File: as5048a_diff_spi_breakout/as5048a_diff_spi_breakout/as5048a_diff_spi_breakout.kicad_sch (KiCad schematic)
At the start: 8 parts, among them J1 Conn_01x02, J2 8P8C, U1 SN65LVDT14, U2 AS5048A

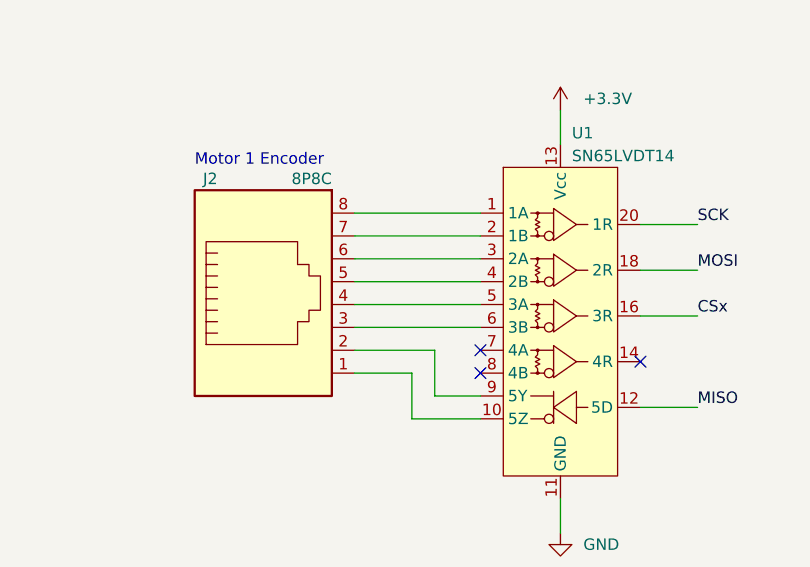
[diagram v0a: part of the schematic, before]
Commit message: adding pareto leg kins
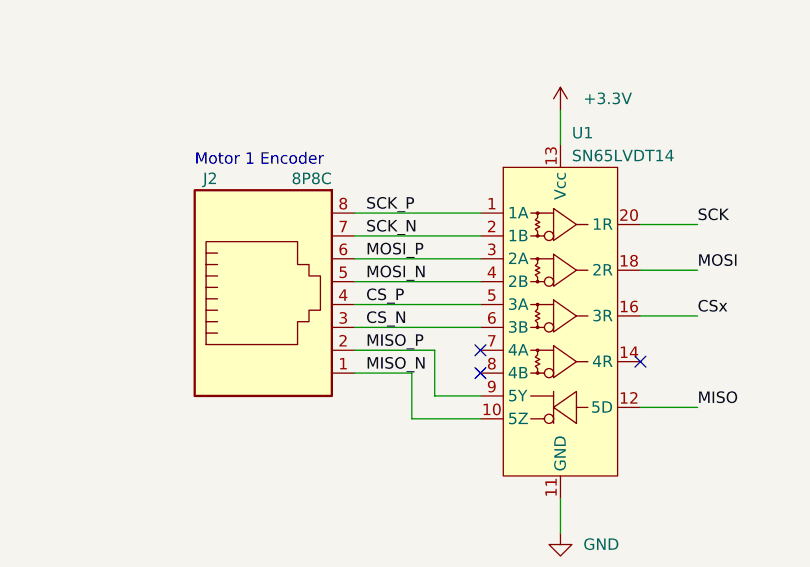
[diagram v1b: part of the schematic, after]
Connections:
- net SCK_P: now reaches J2.8, U1.1 (1A)
- net MISO_N: now reaches J2.1, U1.10 (5Z)
- net SCK_N: now reaches J2.7, U1.2 (1B)
- net MOSI_P: now reaches J2.6, U1.3 (2A)
- net MOSI_N: now reaches J2.5, U1.4 (2B)
- net CS_P: now reaches J2.4, U1.5 (3A)
- net CS_N: now reaches J2.3, U1.6 (3B)
- net MISO_P: now reaches J2.2, U1.9 (5Y)
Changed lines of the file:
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@@
+    (effects (font (size 1.27 1.27)) (justify left bottom))
+  )
+  (label "MISO_P" (at 105.41 97.79 0)
     (effects (font (size 1.27 1.27)) (justify left bottom))
   )
@@
   )
   (label "CSx" (at 142.24 93.98 0)
+    (effects (font (size 1.27 1.27)) (justify left bottom))
+  )
+  (label "MISO_N" (at 105.41 100.33 0)
     (effects (font (size 1.27 1.27)) (justify left bottom))
   )
@@
     (effects (font (size 1.27 1.27)) (justify left bottom))
   )
+  (label "SCK_N" (at 105.41 85.09 0)
+    (effects (font (size 1.27 1.27)) (justify left bottom))
+  )
   (label "MISO" (at 142.24 104.14 0)
+    (effects (font (size 1.27 1.27)) (justify left bottom))
+  )
+  (label "CS_P" (at 105.41 92.71 0)
+    (effects (font (size 1.27 1.27)) (justify left bottom))
+  )
+  (label "CS_N" (at 105.41 95.25 0)
+    (effects (font (size 1.27 1.27)) (justify left bottom))
+  )
+  (label "MOSI_N" (at 105.41 90.17 0)
     (effects (font (size 1.27 1.27)) (justify left bottom))
   )
@@
     (effects (font (size 1.27 1.27)) (justify left bottom))
   )
+  (label "SCK_P" (at 105.41 82.55 0)
+    (effects (font (size 1.27 1.27)) (justify left bottom))
+  )
+  (label "MOSI_P" (at 105.41 87.63 0)
+    (effects (font (size 1.27 1.27)) (justify left bottom))
+  )
